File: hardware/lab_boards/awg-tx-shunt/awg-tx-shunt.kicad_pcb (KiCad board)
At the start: 2 copper layers, 66 x 57.1 mm, 18 parts, among them J1 FROM PWR AMP, J2 TX, J3 SHUNT

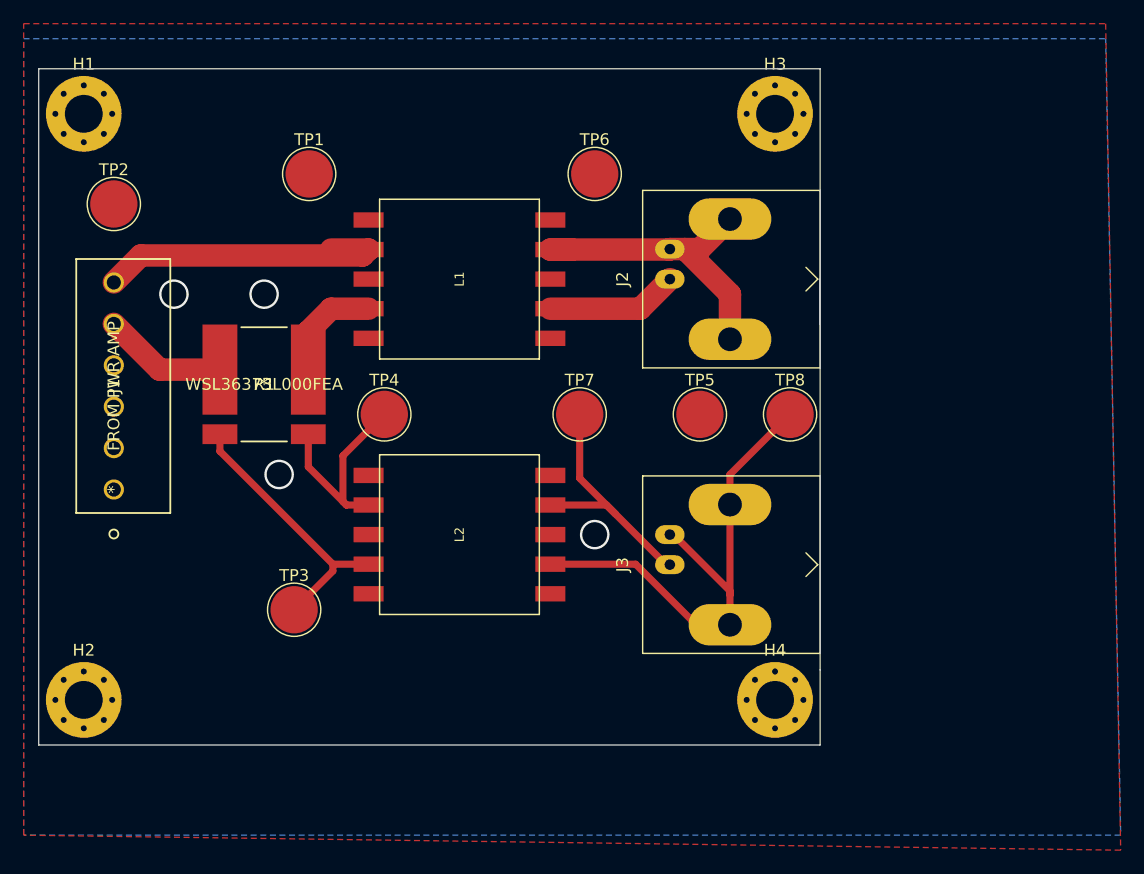
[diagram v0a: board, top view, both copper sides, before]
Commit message: Added identifier text, warning symbols, and chamfered edges to the edge cuts, and rerouted wiring under the BNC connectors.
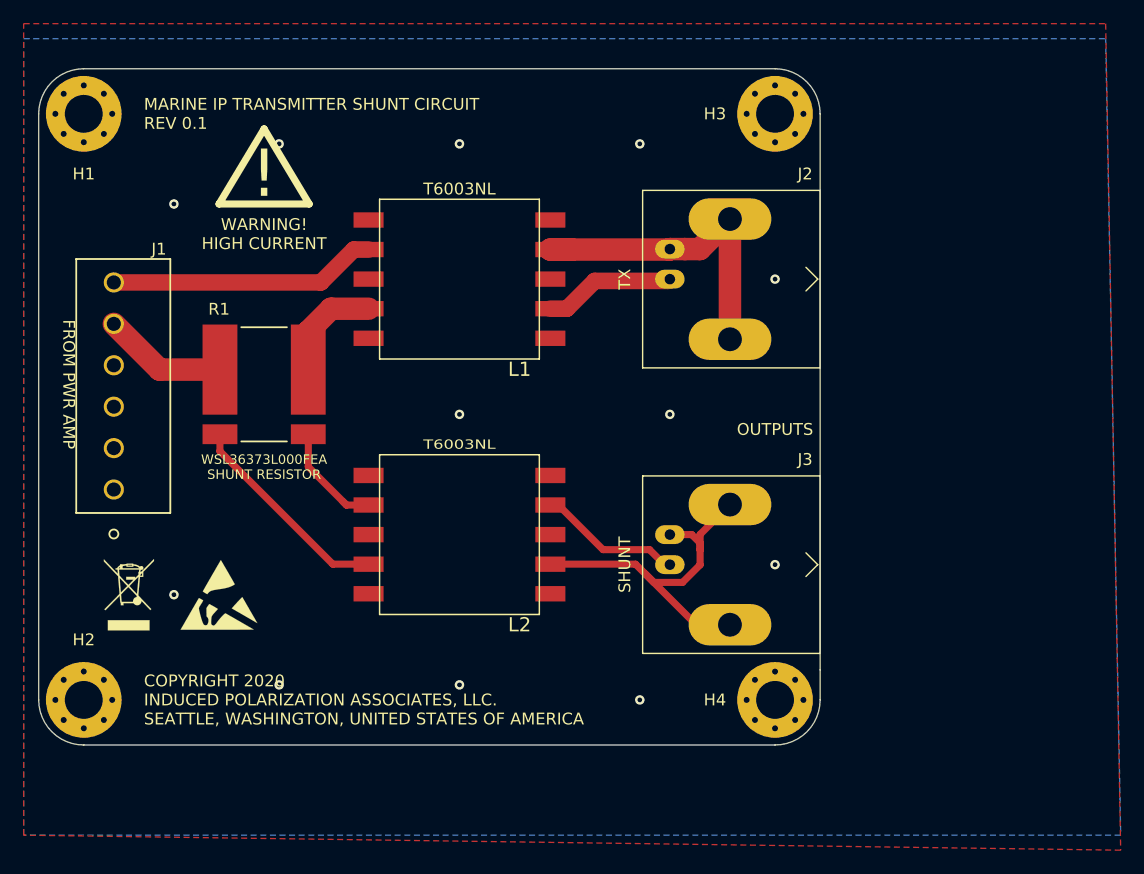
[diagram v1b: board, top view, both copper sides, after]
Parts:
- removed TP1, TP2, TP3, TP4, TP5, TP6, TP7, TP8: TestPoint, TestPoint:TestPoint_Pad_D4.0mm
- added REF**: ESD-Logo_6.6x6mm_SilkScreen, Symbol:ESD-Logo_6.6x6mm_SilkScreen, F.Cu at (91.4, 120.7)
- added REF**: WEEE-Logo_4.2x6mm_SilkScreen, Symbol:WEEE-Logo_4.2x6mm_SilkScreen, F.Cu at (83.8, 120.7)
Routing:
- net Net-(J3-Pad1): track 21.8 -> 12.5 mm
- net Net-(J3-Pad2): track 44.6 -> 35.6 mm
- net /SHUNT_N: track 18.4 -> 9.61 mm
- net /SHUNT_P: track 23.2 -> 18.0 mm
- net /TX1: track 25.9 -> 22.7 mm
- net Net-(J2-Pad2): track 27.3 -> 28.3 mm
- net GNDPWR: vias 4 -> 12
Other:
- outline, holes or cut-outs redrawn
- net class shunt: clearance 0.6 -> 0.4
- net class sigpwr: trace_width 1.9 -> 1.4
- board text added: "!"
- board text added: "COPYRIGHT 2020 INDUCED POLARIZATION ASSOCIATES, LLC. SEATTLE, WASHINGTON, UNITED STATES OF AMERICA"
- board text added: "MARINE IP TRANSMITTER SHUNT CIRCUIT REV 0.1"
- board text added: "OUTPUTS"
- board text added: "SHUNT RESISTOR"
- board text added: "WARNING! HIGH CURRENT"
